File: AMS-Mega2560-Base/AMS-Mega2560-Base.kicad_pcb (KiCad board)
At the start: 4 copper layers, 168.7 x 106.7 mm, 210 parts, among them IC1 CD74HC4050ME4, IC10 LM2597MX-ADJ_NOPB, IC11 LM2597M-3.3_NOPB, IC12 OPA2340PA, IC13 MAX764CPA+, IC14 LM2917N-8_NOPB, IC15 MAX31865AAP+, IC16 DS3231SN#, IC17 MAX232CPE+, IC18 MAX31865AAP+, IC2 CD74HC4050ME4, IC3 MAX31865AAP+, IC4 MAX31865AAP+, IC5 MAX31865AAP+, IC6 OPA2340PA, IC7 LTV-846S, IC8 MAX31865AAP+, IC9 LM2670SX-5.0_NOPB, J1 RTD1, J10 Conn_01x03, J11 Conn_01x02, J12 Conn_01x02, J13 Conn_01x03, J14 Conn_01x02, J15 Conn_01x02, J16 Conn_01x03, J17 Conn_01x02, J18 Conn_01x02, J19 Conn_01x03, J2 RTD2, J20 Conn_01x02, J21 Screw_Terminal_01x02, J22 Conn_01x06, J23 Conn_01x02, J24 Conn_01x02, J25 Conn_01x02, J26 Conn_01x03, J27 Conn_01x02, J28 Conn_01x02, J29 Conn_01x03, J3 Conn_01x08, J30 Conn_01x02, J31 Conn_01x02, J32 Conn_01x02, J4 Sense1, J5 Sense2, J6 AdafruitUltimateGPS, J7 Conn_02x03_Odd_Even, J8 Conn_01x03, J9 Conn_01x02, P1 Power, P10 CONN_01X01, P11 CONN_01X01, P12 CONN_01X01, P13 CONN_01X01, P2 Analog, P3 Analog, P4 Digital, P5 PWM, P6 PWM, P7 Communication, P8 CONN_01X01, P9 CONN_01X01, Q1 2N7000, Q10 IRF9Z34NPBF, Q11 2N7000, Q12 2N7000, Q13 IRF9Z34NPBF, Q14 IRF9Z34NPBF, Q15 2N7000, Q16 2N7000, Q17 IRF9Z34NPBF, Q18 IRF9Z34NPBF, Q19 2N7000, Q2 2N7000, Q20 IRF9Z34NPBF, Q3 2N7000, Q4 2N7000, Q6 IRF9Z34NPBF, Q7 2N7000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

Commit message: I think everything is placed on the board special routes have been done. need to finish routing everything else.
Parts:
- added J33: Conn_01x02, Connector_PinHeader_2.54mm:PinHeader_1x02_P2.54mm_Vertical, F.Cu at (154.1, 122.3)
- C1, C2, C33, C34, C4, C5, C7, C8: moved to B.Cu
- moved R4 237.3 mm to (157.9, 129.2)
- moved C9 228.5 mm to (158.7, 142.2), turned to 90 degrees
- moved J15 228.1 mm to (163.3, 138.7)
- moved C8 216.6 mm to (166.2, 129.4)
- moved J16 216.2 mm to (170.7, 138.7)
- moved J17 215.9 mm to (167.0, 138.7)
- moved C7 211.2 mm to (166.3, 132.7), turned to 0 degrees
- moved IC5 205.4 mm to (166.3, 131.7)
- moved C35 199.5 mm to (207.3, 148.9), turned to 90 degrees
- moved R36 197.3 mm to (206.3, 136.1)
- moved J25 194.0 mm to (212.1, 145.1)
- moved J26 184.6 mm to (219.5, 145.1)
- moved J27 178.9 mm to (215.8, 145.1)
- moved C33 177.9 mm to (215.1, 139.8), turned to 0 degrees
- moved C34 175.1 mm to (215.2, 136.5)
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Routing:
- net Net-(Q6-Pad1): track 7.29 -> 0.00 mm
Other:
- board text added: "Ambient Temp"
- board text added: "CARB Temp"
- board text added: "Front Temp"
- board text added: "Right Side Temp"

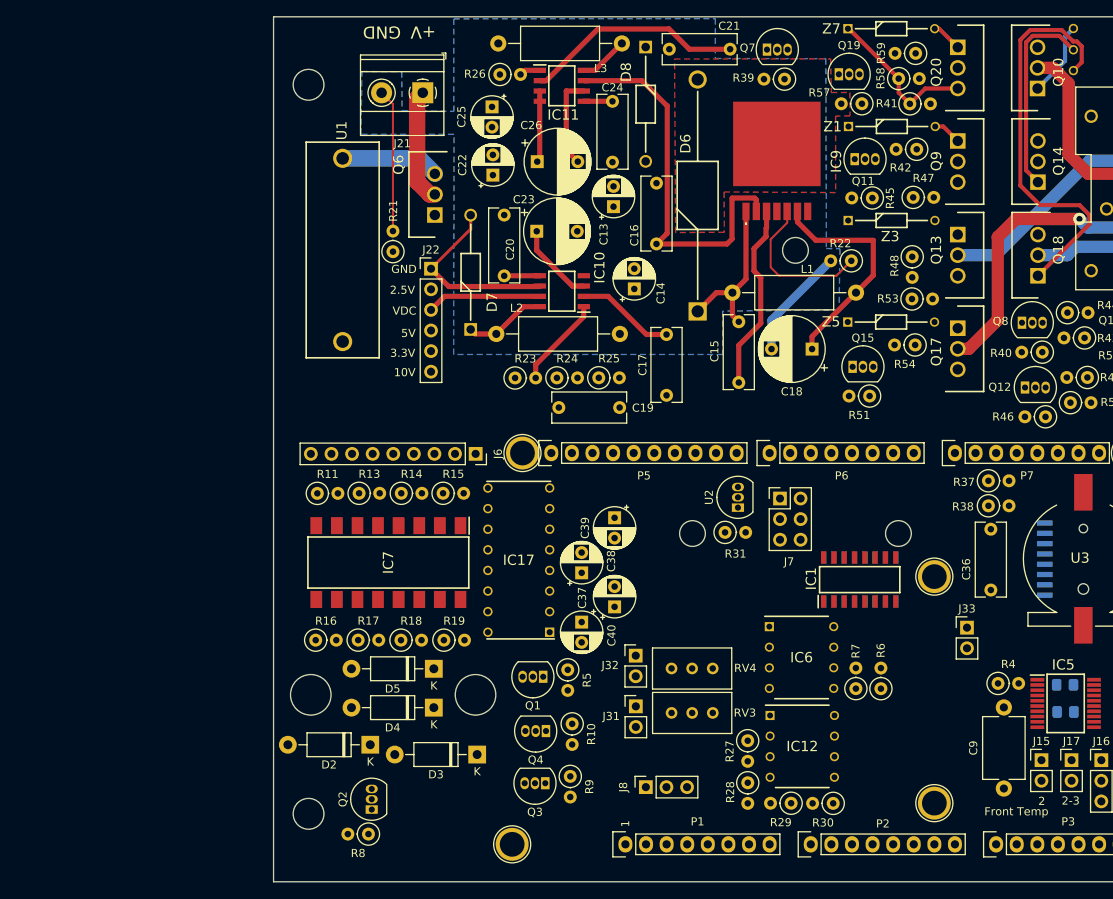
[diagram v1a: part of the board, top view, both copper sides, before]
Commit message: WIP for power on input and RTC battery switch over.
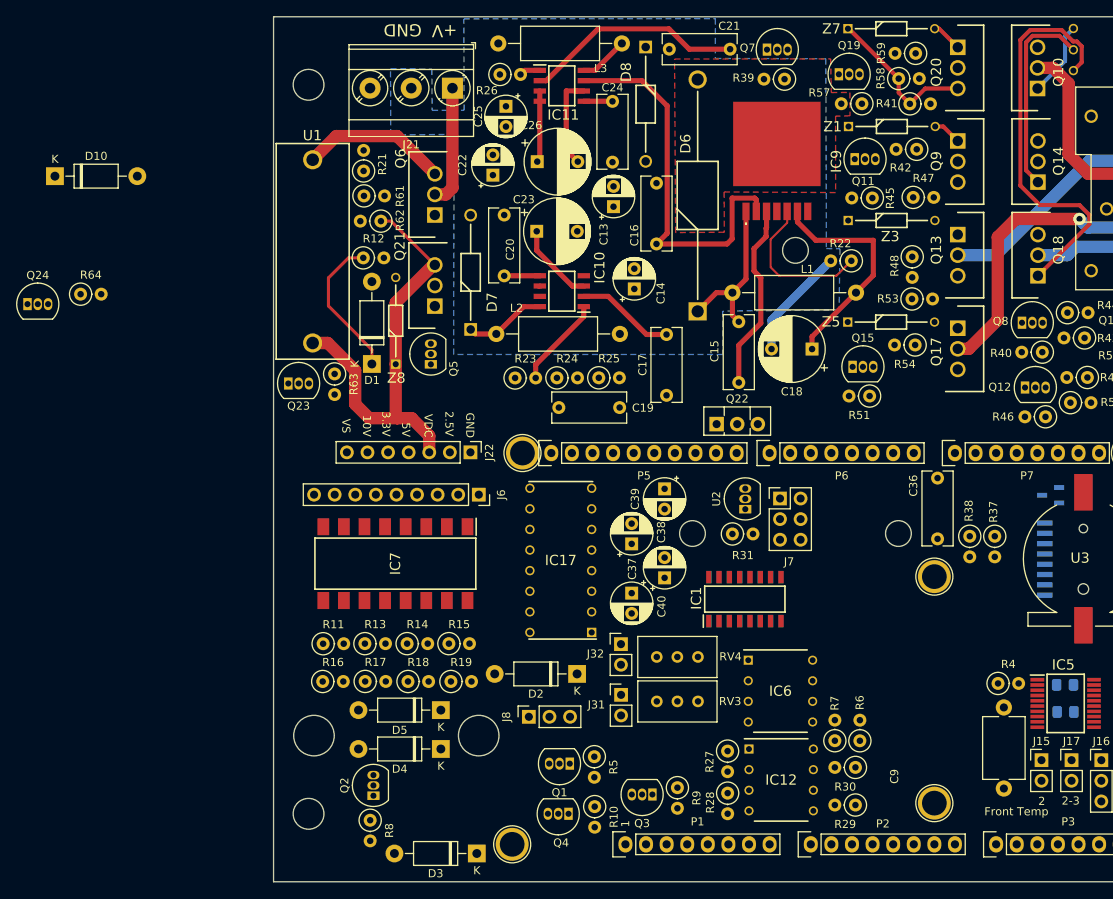
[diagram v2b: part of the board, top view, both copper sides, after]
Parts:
- removed J33: Conn_01x02, Connector_PinHeader_2.54mm:PinHeader_1x02_P2.54mm_Vertical
- added D1: 1N4007, Diode_THT:D_DO-41_SOD81_P10.16mm_Horizontal, F.Cu at (80.7, 89.8)
- added D10: 1N4001, Diode_THT:D_DO-41_SOD81_P10.16mm_Horizontal, F.Cu at (41.6, 66.6)
- added IC19: MAX6326UR31+T, SamacSys_Parts:SOT95P237X112-3N, B.Cu at (164.4, 106.0)
- added Q21: IRF9Z34NPBF, SamacSys_Parts:TO254P469X1042X1967-3P, F.Cu at (88.5, 82.7)
- added Q22: BD140, Package_TO_SOT_THT:TO-126-3_Vertical, F.Cu at (123.2, 97.2)
- added Q23: 2N7000, Package_TO_SOT_THT:TO-92_Inline, F.Cu at (70.4, 92.2)
- added Q24: BS250, Package_TO_SOT_THT:TO-92_Inline, F.Cu at (38.2, 82.4)
- added Q5: 2N7000, Package_TO_SOT_THT:TO-92_Inline, F.Cu at (88.0, 89.8)
- added R12: 1M, Resistor_THT:R_Axial_DIN0207_L6.3mm_D2.5mm_P2.54mm_Vertical, F.Cu at (79.6, 76.7)
- added R61: 10k, Resistor_THT:R_Axial_DIN0207_L6.3mm_D2.5mm_P2.54mm_Vertical, F.Cu at (79.7, 69.1)
- added R62: 100k, Resistor_THT:R_Axial_DIN0207_L6.3mm_D2.5mm_P2.54mm_Vertical, F.Cu at (81.8, 72.2)
- added R63: 1M, Resistor_THT:R_Axial_DIN0207_L6.3mm_D2.5mm_P2.54mm_Vertical, F.Cu at (76.1, 91.0)
- added R64: 4.7K, Resistor_THT:R_Axial_DIN0207_L6.3mm_D2.5mm_P2.54mm_Vertical, F.Cu at (44.8, 81.2)
- added Z8: BZX79C10, SamacSys_Parts:DIOAD1068W53L380D172, F.Cu at (83.6, 89.8)
- J21: value Screw_Terminal_01x02 -> Screw_Terminal_01x03; footprint TerminalBlock_Phoenix:TerminalBlock_Phoenix_MKDS-1,5-2-5.08_1x02_P5.08mm_Horizontal -> TerminalBlock_Phoenix:TerminalBlock_Phoenix_MKDS-3-3-5.08_1x03_P5.08mm_Horizontal
- J22: value Conn_01x06 -> Conn_01x07; footprint Connector_PinHeader_2.54mm:PinHeader_1x06_P2.54mm_Vertical -> Connector_PinHeader_2.54mm:PinHeader_1x07_P2.54mm_Vertical
- moved D2 27.0 mm to (106.0, 128.0)
- moved J22 23.2 mm to (92.9, 100.7), turned to -90 degrees
- moved R11 18.6 mm to (74.7, 124.3)
- moved R13 18.6 mm to (79.8, 124.3)
- moved R14 18.6 mm to (85.1, 124.3)
- moved R15 18.6 mm to (90.2, 124.3)
- moved J8 16.8 mm to (100.1, 133.3)
- moved IC1 14.4 mm to (126.7, 118.8)
- moved IC2 14.4 mm to (126.7, 118.8)
- moved Q3 13.3 mm to (115.3, 142.9)
- moved R9 13.3 mm to (118.4, 142.1)
- moved D3 12.2 mm to (93.6, 150.2)
- moved R5 11.2 mm to (108.1, 138.2)
- moved Q1 11.2 mm to (105.1, 139.1)
- moved R21 10.6 mm to (79.7, 66.0)
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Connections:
- C1 pad 1: +3V3 -> +3.3VA
- C10 pad 1: +3V3 -> +3.3VA
- C11 pad 1: +3V3 -> +3.3VA
- C13 pad 1: +VDC -> +VSW
- C14 pad 1: +VDC -> +VSW
- C16 pad 1: +VDC -> +VSW
- C2 pad 1: +3V3 -> +3.3VA
- C22 pad 1: +VDC -> +VSW
- C33 pad 1: +3V3 -> +3.3VA
- C34 pad 1: +3V3 -> +3.3VA
- C4 pad 1: +3V3 -> +3.3VA
- C41 pad 1: +3V3 -> +3.3VA
- C42 pad 1: +3V3 -> +3.3VA
- C5 pad 1: +3V3 -> +3.3VA
- C7 pad 1: +3V3 -> +3.3VA
- C8 pad 1: +3V3 -> +3.3VA
- IC1 pad 1: +3V3 -> +3.3VA
- IC10 pad 7: +VDC -> +VSW
- IC15 pad 2: +3V3 -> +3.3VA
- IC15 pad 3: +3V3 -> +3.3VA
- IC16 pad 14: /A1 -> Net-(IC16-Pad14)
- IC18 pad 2: +3V3 -> +3.3VA
- IC18 pad 3: +3V3 -> +3.3VA
- IC2 pad 1: +3V3 -> +3.3VA
- IC3 pad 2: +3V3 -> +3.3VA
- IC3 pad 3: +3V3 -> +3.3VA
- IC4 pad 2: +3V3 -> +3.3VA
- IC4 pad 3: +3V3 -> +3.3VA
- IC5 pad 2: +3V3 -> +3.3VA
- IC5 pad 3: +3V3 -> +3.3VA
- IC8 pad 2: +3V3 -> +3.3VA
- IC8 pad 3: +3V3 -> +3.3VA
- IC9 pad 2: +VDC -> +VSW
- J22 pad 5: +3.3VP -> +3.3VA
- R27 pad 1: +VDC -> +VSW
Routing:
- net +VDC: track 337.8 -> 169.9 mm
- net +VSW: track 0.00 -> 92.2 mm
- net GND: track 73.6 -> 33.0 mm
- net Net-(D1-Pad1): track 0.00 -> 18.2 mm
- net +10V: track 64.2 -> 53.5 mm
- net Net-(Q6-Pad3): track 12.2 -> 18.2 mm
- net Net-(J21-Pad1): track 14.1 -> 14.8 mm
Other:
- outline, holes or cut-outs redrawn
- board text added: "VS"

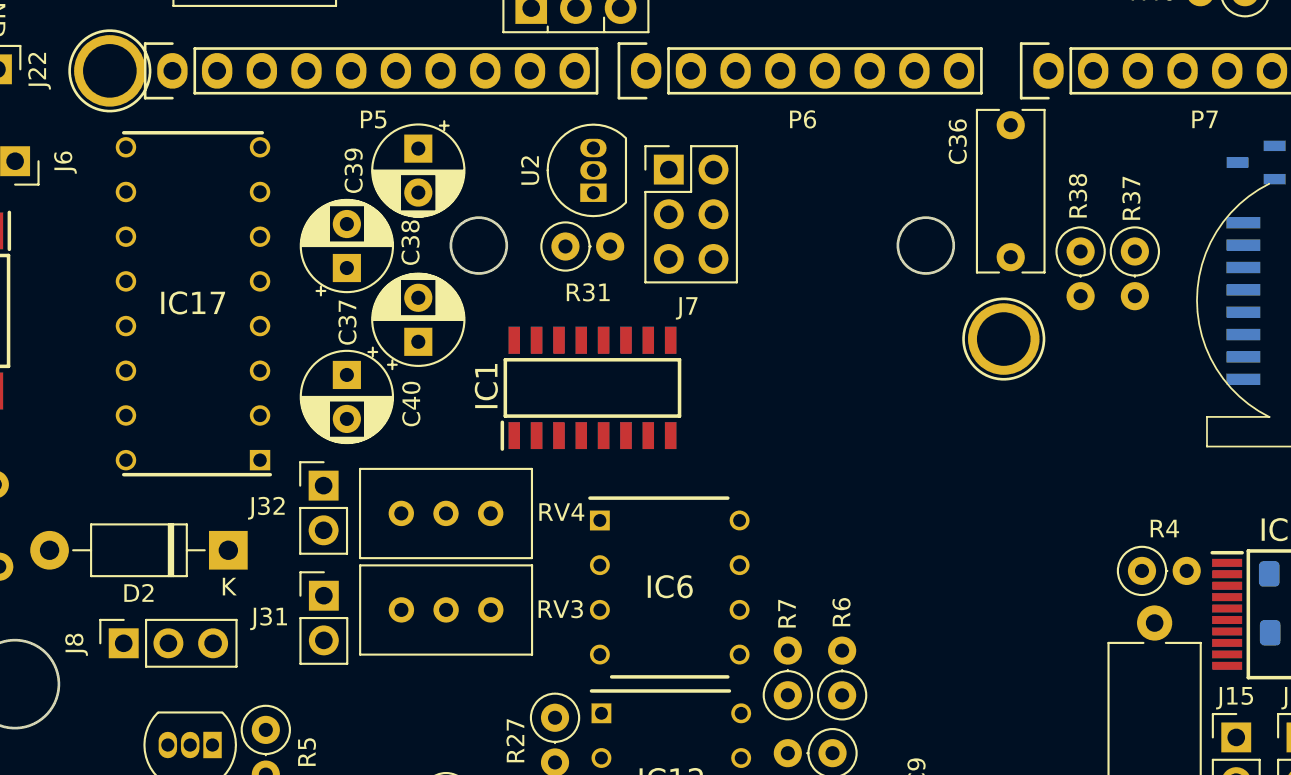
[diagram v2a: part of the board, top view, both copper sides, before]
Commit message: moving some things around on the board to clear the Vacuum board.
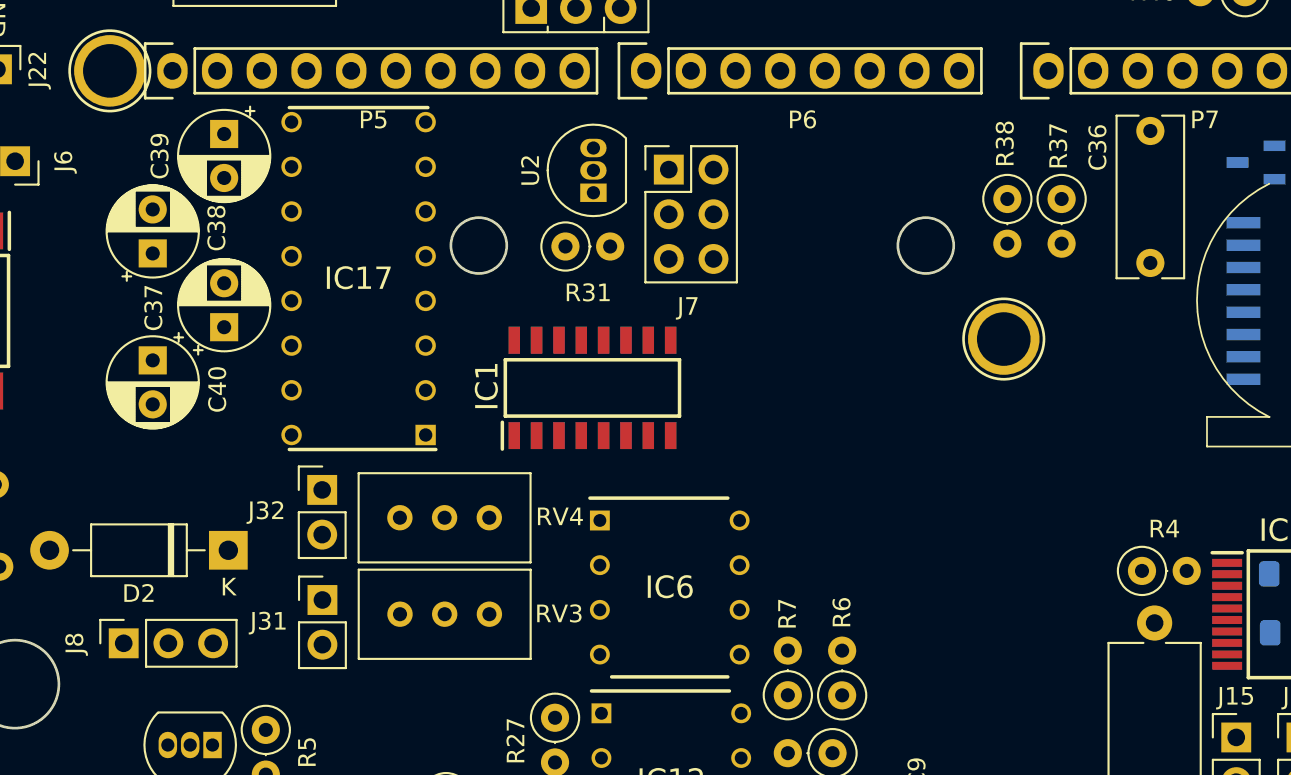
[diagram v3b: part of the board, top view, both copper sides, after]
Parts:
- moved C37 11.1 mm to (105.8, 115.4)
- moved C39 11.1 mm to (105.8, 104.4)
- moved C40 11.1 mm to (101.7, 117.2)
- moved C38 11.1 mm to (101.7, 111.2)
- moved IC17 9.52 mm to (113.4, 112.6)
- moved C36 7.94 mm to (158.4, 104.2)
- moved R37 5.12 mm to (153.4, 108.1)
- moved R38 5.12 mm to (150.3, 108.1)
- moved J31 0.26 mm to (111.4, 130.9)
- moved RV4 0.26 mm to (120.8, 126.2)
- moved J32 0.26 mm to (111.3, 124.6)
- moved RV3 0.26 mm to (120.9, 131.7)
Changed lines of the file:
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@@
   )
   (footprint "Potentiometer_THT:Potentiometer_Bourns_3296W_Vertical" (layer "F.Cu")
-    (at 120.930208 131.424083)
+    (at 120.850014 131.667982)
     (descr "Potentiometer, vertical, Bourns 3296W, https://www.bourns.com/pdfs/3296.pdf")
     (tags "Potentiometer vertical Bourns 3296W")
@@
   )
   (footprint "Resistor_THT:R_Axial_DIN0207_L6.3mm_D2.5mm_P2.54mm_Vertical" (layer "F.Cu")
-    (at 157.532247 111.055595 -90)
+    (at 153.369046 108.072849 -90)
     (descr "Resistor, Axial_DIN0207 series, Axial, Vertical, pin pitch=2.54mm, 0.25W = 1/4W, length*diameter=6.3*2.5mm^2, http://cdn-reichelt.de/documents/datenblatt/B400/1_4W%23YAG.pdf")
     (tags "Resistor Axial_DIN0207 series Axial Vertical pin pitch 2.54mm 0.25W = 1/4W length 6.3mm diameter 2.5mm")
@@
   )
   (footprint "Capacitor_THT:C_Rect_L9.0mm_W3.6mm_P7.50mm_MKT" (layer "F.Cu")
-    (at 150.476577 103.879549 -90)
+    (at 158.411378 104.207199 -90)
     (descr "C, Rect series, Radial, pin pitch=7.50mm, , length*width=9*3.6mm^2, Capacitor, https://en.tdk.eu/inf/20/20/db/fc_2009/MKT_B32560_564.pdf")
     (tags "C Rect series Radial pin pitch 7.50mm  length 9mm width 3.6mm Capacitor")
@@
   )
   (footprint "Capacitor_THT:CP_Radial_D5.0mm_P2.50mm" (layer "F.Cu")
-    (at 116.810288 105.207749 -90)
+    (at 105.777591 104.378775 -90)
     (descr "CP, Radial series, Radial, pin pitch=2.50mm, , diameter=5mm, Electrolytic Capacitor")
     (tags "CP Radial series Radial pin pitch 2.50mm  diameter 5mm Electrolytic Capacitor")
@@
   )
   (footprint "Capacitor_THT:CP_Radial_D5.0mm_P2.50mm" (layer "F.Cu")
-    (at 112.7509 118.072149 -90)
+    (at 101.718203 117.243175 -90)
     (descr "CP, Radial series, Radial, pin pitch=2.50mm, , diameter=5mm, Electrolytic Capacitor")
     (tags "CP Radial series Radial pin pitch 2.50mm  diameter 5mm Electrolytic Capacitor")
@@
   )
   (footprint "Connector_PinHeader_2.54mm:PinHeader_1x02_P2.54mm_Vertical" (layer "F.Cu")
-    (at 111.442305 130.616589)
+    (at 111.362111 130.860488)
     (descr "Through hole straight pin header, 1x02, 2.54mm pitch, single row")
     (tags "Through hole pin header THT 1x02 2.54mm single row")
@@
   )
   (footprint "SamacSys_Parts:DIP762W56P254L1918H457Q16N" (layer "F.Cu")
-    (at 104.006204 114.024413 180)
+    (at 113.417007 112.593659 180)
     (descr "16 PDIP")
     (tags "Integrated Circuit")
@@
   )
   (footprint "Capacitor_THT:CP_Radial_D5.0mm_P2.50mm" (layer "F.Cu")
-    (at 112.7509 111.995134 90)
+    (at 101.718203 111.16616 90)
     (descr "CP, Radial series, Radial, pin pitch=2.50mm, , diameter=5mm, Electrolytic Capacitor")
     (tags "CP Radial series Radial pin pitch 2.50mm  diameter 5mm Electrolytic Capacitor")
@@
   )
   (footprint "Resistor_THT:R_Axial_DIN0207_L6.3mm_D2.5mm_P2.54mm_Vertical" (layer "F.Cu")
-    (at 154.447822 111.055595 -90)
+    (at 150.284621 108.072849 -90)
     (descr "Resistor, Axial_DIN0207 series, Axial, Vertical, pin pitch=2.54mm, 0.25W = 1/4W, length*diameter=6.3*2.5mm^2, http://cdn-reichelt.de/documents/datenblatt/B400/1_4W%23YAG.pdf")
     (tags "Resistor Axial_DIN0207 series Axial Vertical pin pitch 2.54mm 0.25W = 1/4W length 6.3mm diameter 2.5mm")
@@
   )
   (footprint "Capacitor_THT:CP_Radial_D5.0mm_P2.50mm" (layer "F.Cu")
-    (at 116.810288 116.187768 90)
+    (at 105.777591 115.358794 90)
     (descr "CP, Radial series, Radial, pin pitch=2.50mm, , diameter=5mm, Electrolytic Capacitor")
     (tags "CP Radial series Radial pin pitch 2.50mm  diameter 5mm Electrolytic Capacitor")
@@
   )
   (footprint "Connector_PinHeader_2.54mm:PinHeader_1x02_P2.54mm_Vertical" (layer "F.Cu")
-    (at 111.428722 124.361268)
+    (at 111.348528 124.605167)
     (descr "Through hole straight pin header, 1x02, 2.54mm pitch, single row")
     (tags "Through hole pin header THT 1x02 2.54mm single row")
@@
   )
   (footprint "Potentiometer_THT:Potentiometer_Bourns_3296W_Vertical" (layer "F.Cu")
-    (at 120.923786 125.941298)
+    (at 120.843592 126.185197)
     (descr "Potentiometer, vertical, Bourns 3296W, https://www.bourns.com/pdfs/3296.pdf")
     (tags "Potentiometer vertical Bourns 3296W")
